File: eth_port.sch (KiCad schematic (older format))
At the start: 19 parts, among them U201 LAN8810

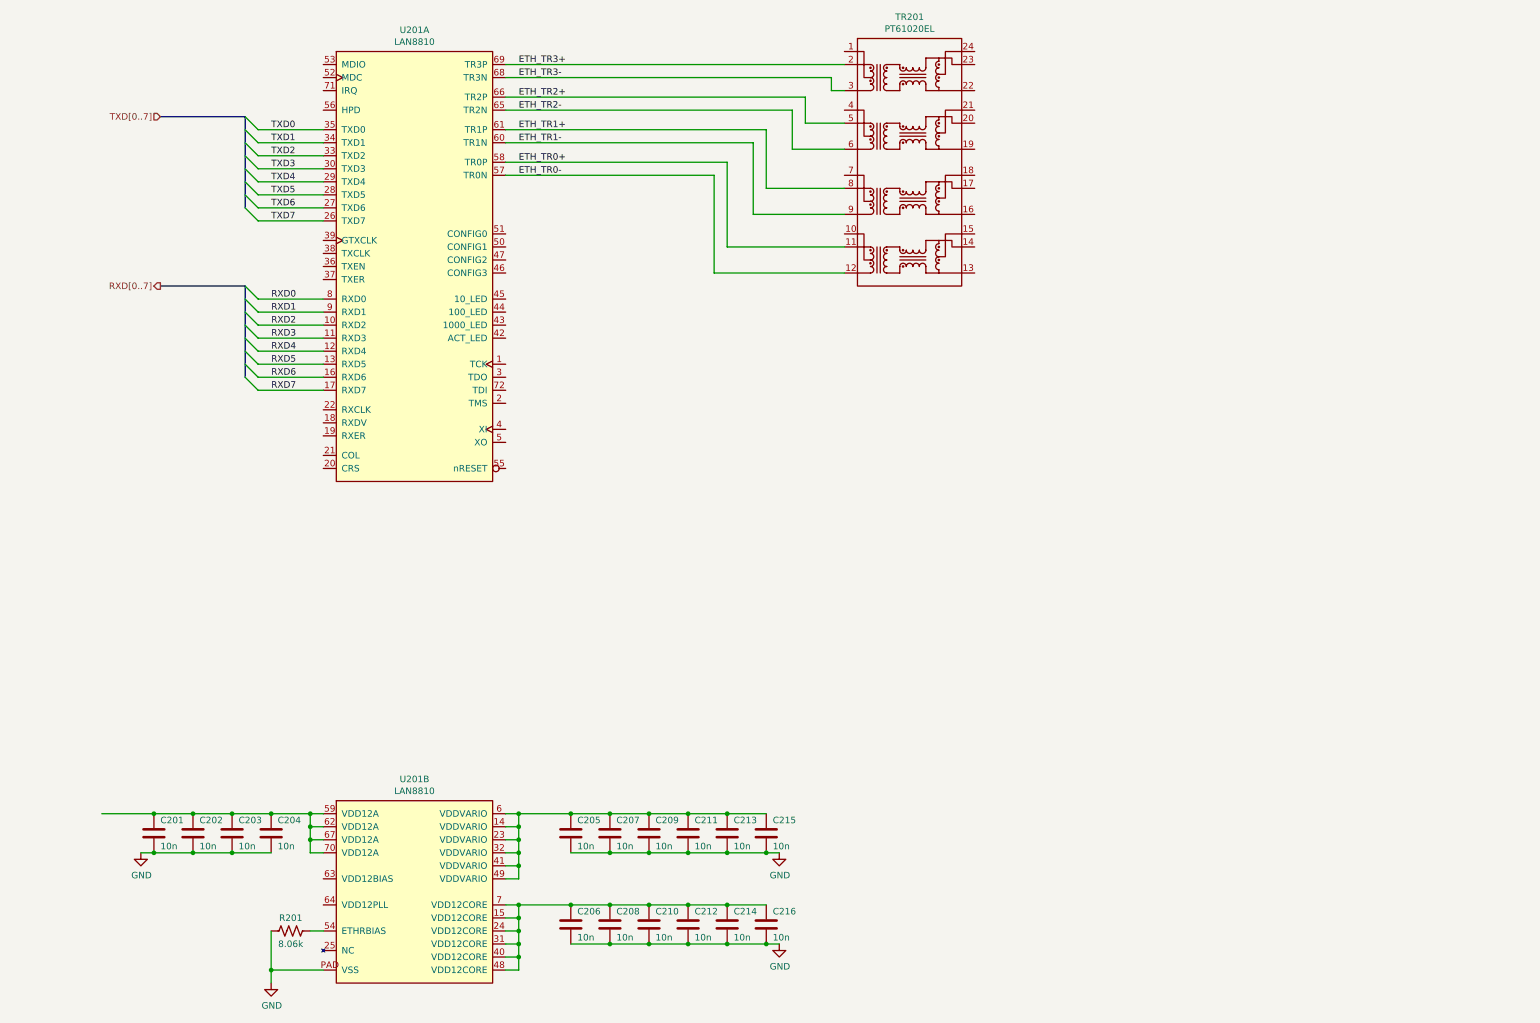
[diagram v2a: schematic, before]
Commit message: - Selected a shielded RJ45 with dual LEDs, with the cable orientation such   that it makes the transformer-to-RJ45 wiring nice. - Added a second whole Ethernet port and connected the two ports together at   the top level.
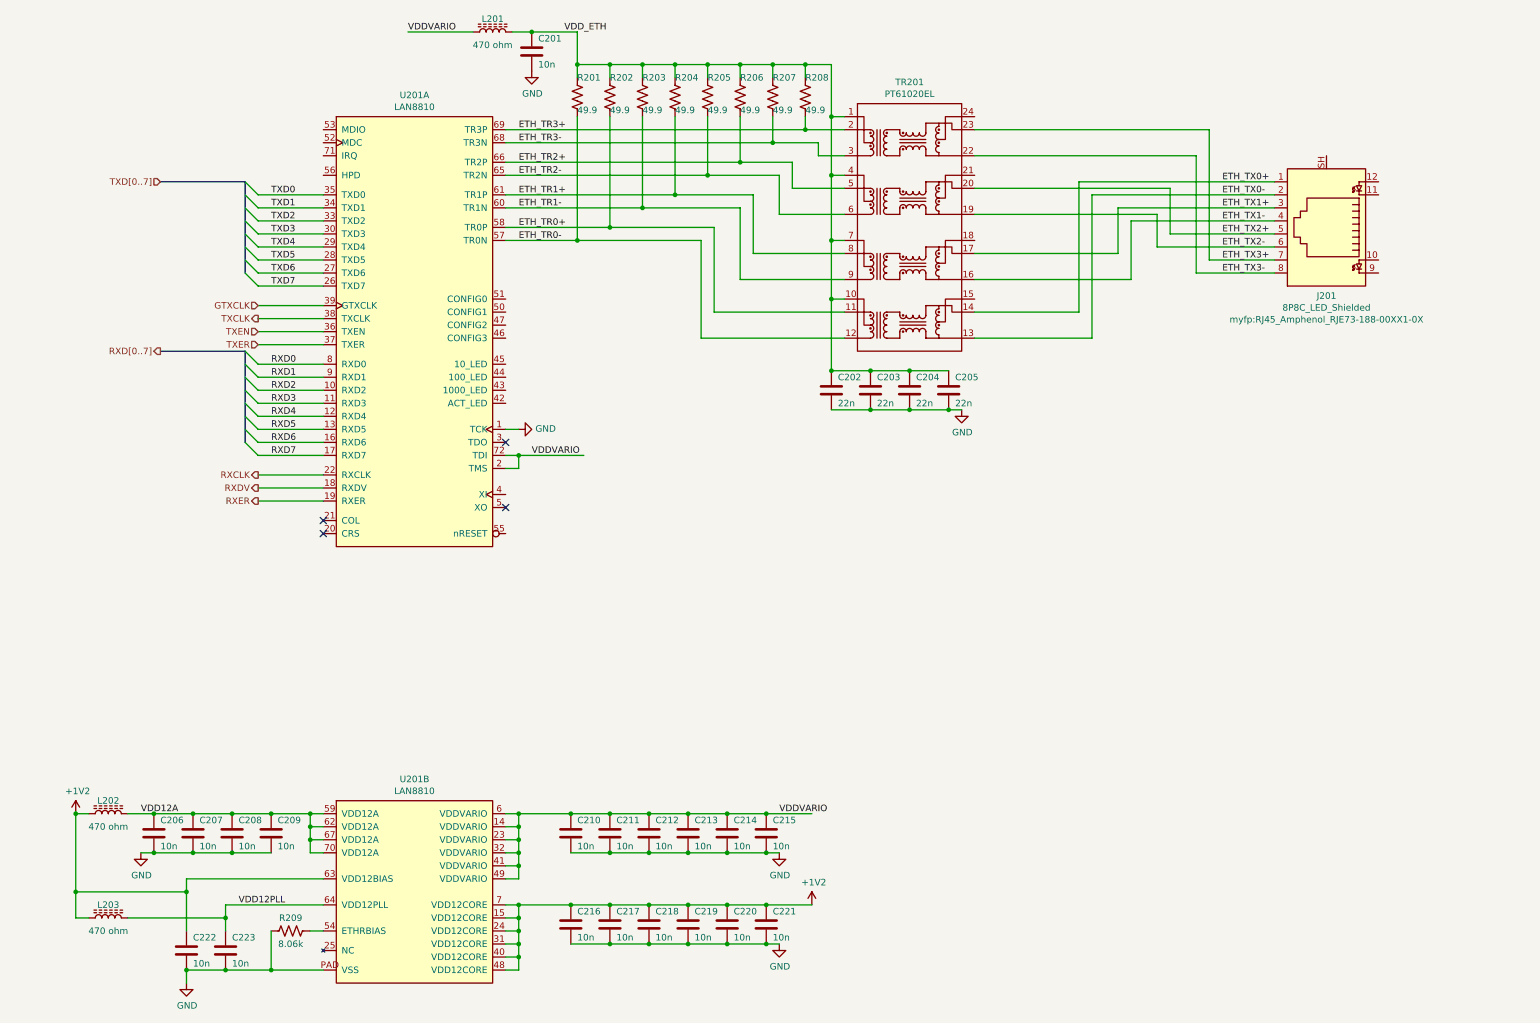
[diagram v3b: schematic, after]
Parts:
- added C301, C322, C323: 10n, Capacitor_SMD:C_0603_1608Metric, symbol Device:C
- added C302, C303, C304, C305: 22n, Capacitor_SMD:C_0603_1608Metric, symbol Device:C
- added J301: 8P8C_LED_Shielded, myfp:RJ45_Amphenol_RJE73-188-00XX1-0X, symbol Connector:8P8C_LED_Shielded
- added L301, L302, L303: 470 ohm, Inductor_SMD:L_0603_1608Metric, symbol Device:L_Core_Ferrite
- added R301, R302, R303, R304, R305, R306, R307, R308: 49.9, Resistor_SMD:R_0603_1608Metric, symbol Device:R_US
- renumbered C201 to C306, C202 to C307, C203 to C308, C204 to C309, C205 to C310, C207 to C311, C209 to C312, C211 to C313, C213 to C314, C215 to C315, C206 to C316, C208 to C317, C210 to C318, C212 to C319, C214 to C320, C216 to C321, R201 to R309, TR201 to TR301, U201 to U301
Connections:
- net ETH_TR0+: now also R302.2
- net ETH_TR0-: now also R301.2
- net ETH_TR1+: now also R304.2
- net ETH_TR1-: now also R303.2
- net ETH_TR2+: now also R306.2
- net ETH_TR2-: now also R305.2
- net ETH_TR3+: now also R308.2
- net ETH_TR3-: now also R307.2
- net GND: now also U301.1 (TCK), C301.2, C302.2, C303.2, C304.2, C305.2, C322.2, C323.2
- net RXDV: now reaches U301.18 (RXDV)
- net RXER: now reaches U301.19 (RXER)
- net VDDVARIO: now reaches U301.2 (TMS)
- net VDDVARIO: now also C310.1, C311.1, C312.1, C313.1, C314.1, C315.1, U301.14 (VDDVARIO), U301.23 (VDDVARIO), U301.32 (VDDVARIO), U301.41 (VDDVARIO), U301.49 (VDDVARIO), U301.6 (VDDVARIO), U301.72 (TDI), L301.1
- net RXCLK: now reaches U301.22 (RXCLK)
- net TXEN: now reaches U301.36 (TXEN)
- net TXER: now reaches U301.37 (TXER)
- net TXCLK: now reaches U301.38 (TXCLK)
- net GTXCLK: now reaches U301.39 (GTXCLK)
- net +1V2: now reaches C316.1, C317.1, C318.1, C319.1, C320.1, C321.1, U301.15 (VDD12CORE), U301.24 (VDD12CORE), U301.31 (VDD12CORE), U301.40 (VDD12CORE), U301.48 (VDD12CORE), U301.7 (VDD12CORE)
- net +1V2: now also U301.63 (VDD12BIAS), C322.1, L302.1, L303.1
- net VDD12A: now reaches C306.1, C307.1, C308.1, C309.1, U301.59 (VDD12A), U301.62 (VDD12A), U301.67 (VDD12A), U301.70 (VDD12A)
- net VDD12A: now also L302.2
- net VDD12PLL: now reaches U301.64 (VDD12PLL)
- net VDD12PLL: now also C323.1, L303.2
- net VDD_ETH: now reaches TR301.1 (TCT1)
- net VDD_ETH: now also TR301.10 (TCT4), TR301.4 (TCT2), TR301.7 (TCT3), C301.1, C302.1, C303.1, C304.1, C305.1, L301.2, R301.1, R302.1, R303.1, R304.1, R305.1, R306.1, R307.1, R308.1
- net ETH_TX0-: now reaches TR301.13 (MX4-)
- net ETH_TX0-: now also J301.2
- net ETH_TX0+: now reaches TR301.14 (MX4+)
- net ETH_TX0+: now also J301.1
- net ETH_TX1-: now reaches TR301.16 (MX3-)
- net ETH_TX1-: now also J301.4
- net ETH_TX1+: now reaches TR301.17 (MX3+)
- net ETH_TX1+: now also J301.3
- net ETH_TX2-: now reaches TR301.19 (MX2-)
- net ETH_TX2-: now also J301.6
- net ETH_TX2+: now reaches TR301.20 (MX2+)
- net ETH_TX2+: now also J301.5
- net ETH_TX3-: now reaches TR301.22 (MX1-)
- net ETH_TX3-: now also J301.8
- net ETH_TX3+: now reaches TR301.23 (MX1+)
- net ETH_TX3+: now also J301.7
- no-connect marks 0 -> 4
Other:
- moved on the sheet: TR201, U201A

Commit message: - Added termination network to line side of Ethernet transformer - Started vaguely laying out the big pieces of Ethernet1 block - Set PCB layout to be six layers - Added layout layer identification texts
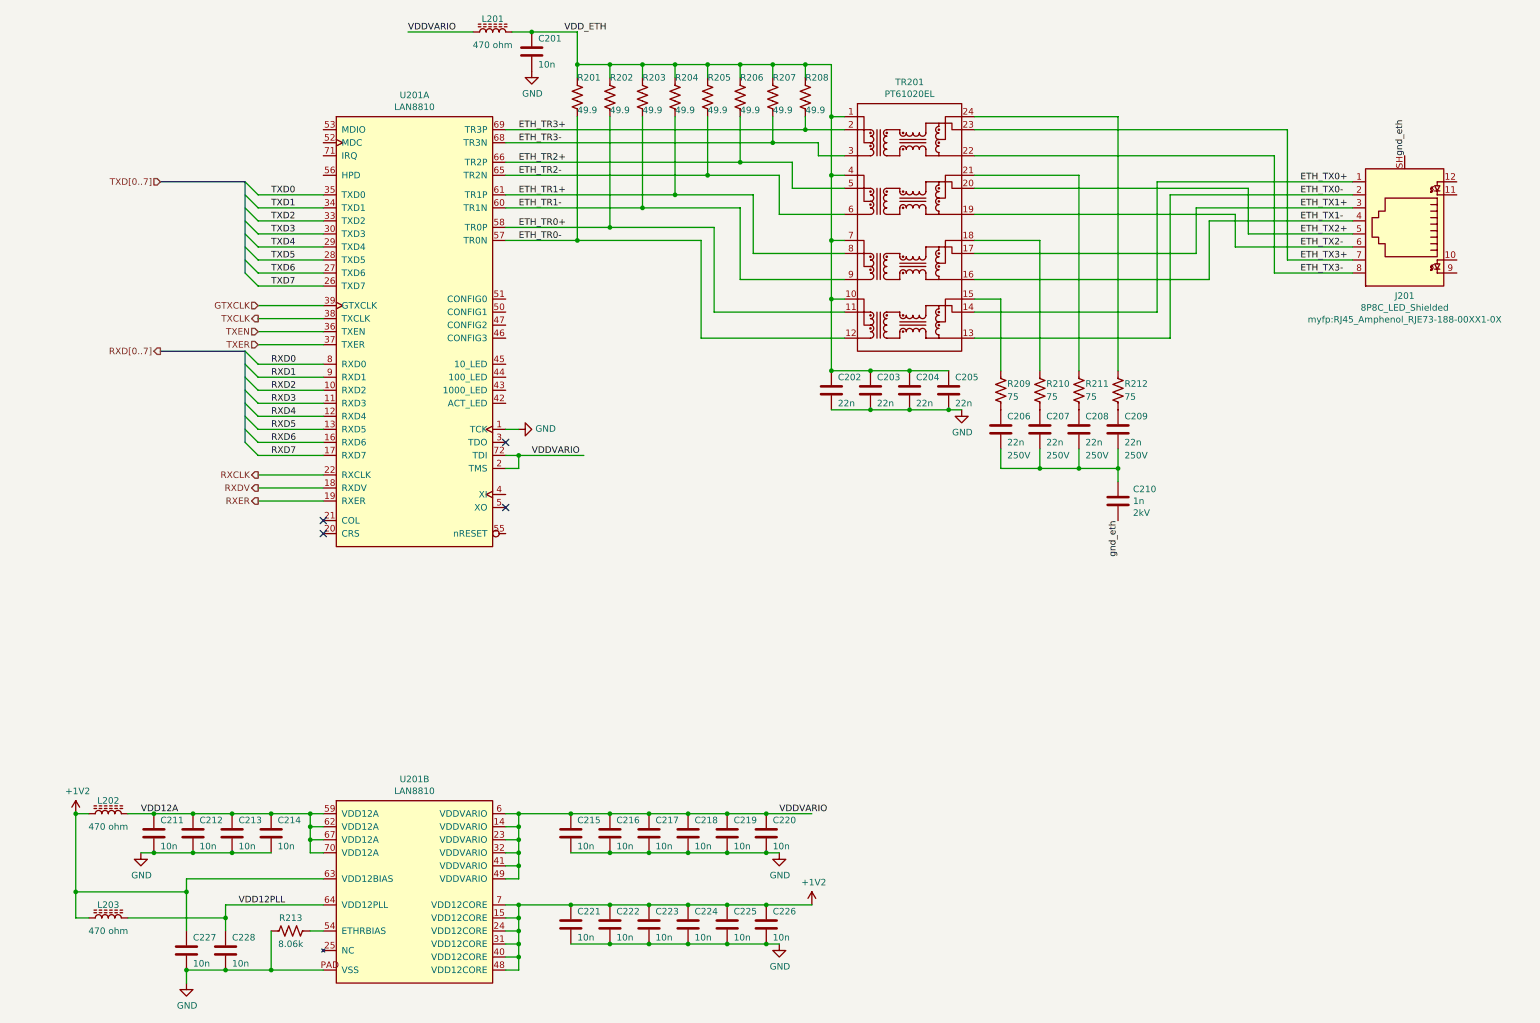
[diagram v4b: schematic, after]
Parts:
- added C206, C207, C208, C209: 22n, Capacitor_SMD:C_0805_2012Metric, symbol Device:C
- added C210: 1n, Capacitor_SMD:C_1206_3216Metric, symbol Device:C
- added R209, R210, R211, R212: 75, Resistor_SMD:R_0603_1608Metric, symbol Device:R_US
- renumbered C306 to C311, C307 to C312, C308 to C313, C309 to C314, C310 to C315, C311 to C316, C312 to C317, C313 to C318, C314 to C319, C315 to C320, C316 to C321, C317 to C322, C318 to C323, C319 to C324, C320 to C325, C321 to C326, C322 to C327, C323 to C328, R309 to R313
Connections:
- net at TR301.15 (MCT4): now also R209.1
- net at TR301.18 (MCT3): now also R210.1
- net at TR301.21 (MCT2): now also R211.1
- net at TR301.24 (MCT1): now also R212.1
- net gnd_eth: now reaches J301.SH
- net gnd_eth: now also C210.2
- new net: C206.1, R209.2
- new net: C206.2, C207.2, C208.2, C209.2, C210.1
- new net: C207.1, R210.2
- new net: C208.1, R211.2
- new net: C209.1, R212.2
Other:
- moved on the sheet: J201

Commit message: - Adjusted RJ45 main pin thru-holes to have only an 8mil-wide ring, instead of   10mil.  There was just not enough room for routing. - Fixed wiring to RJ45, it was 3/4 and 5/6 instead of 3/6 and 4/5, whoops! - Set up basic board routing parameters including diff pairs - Routed the Ethernet1 transformer-to-RJ45 area as proof-of-concept
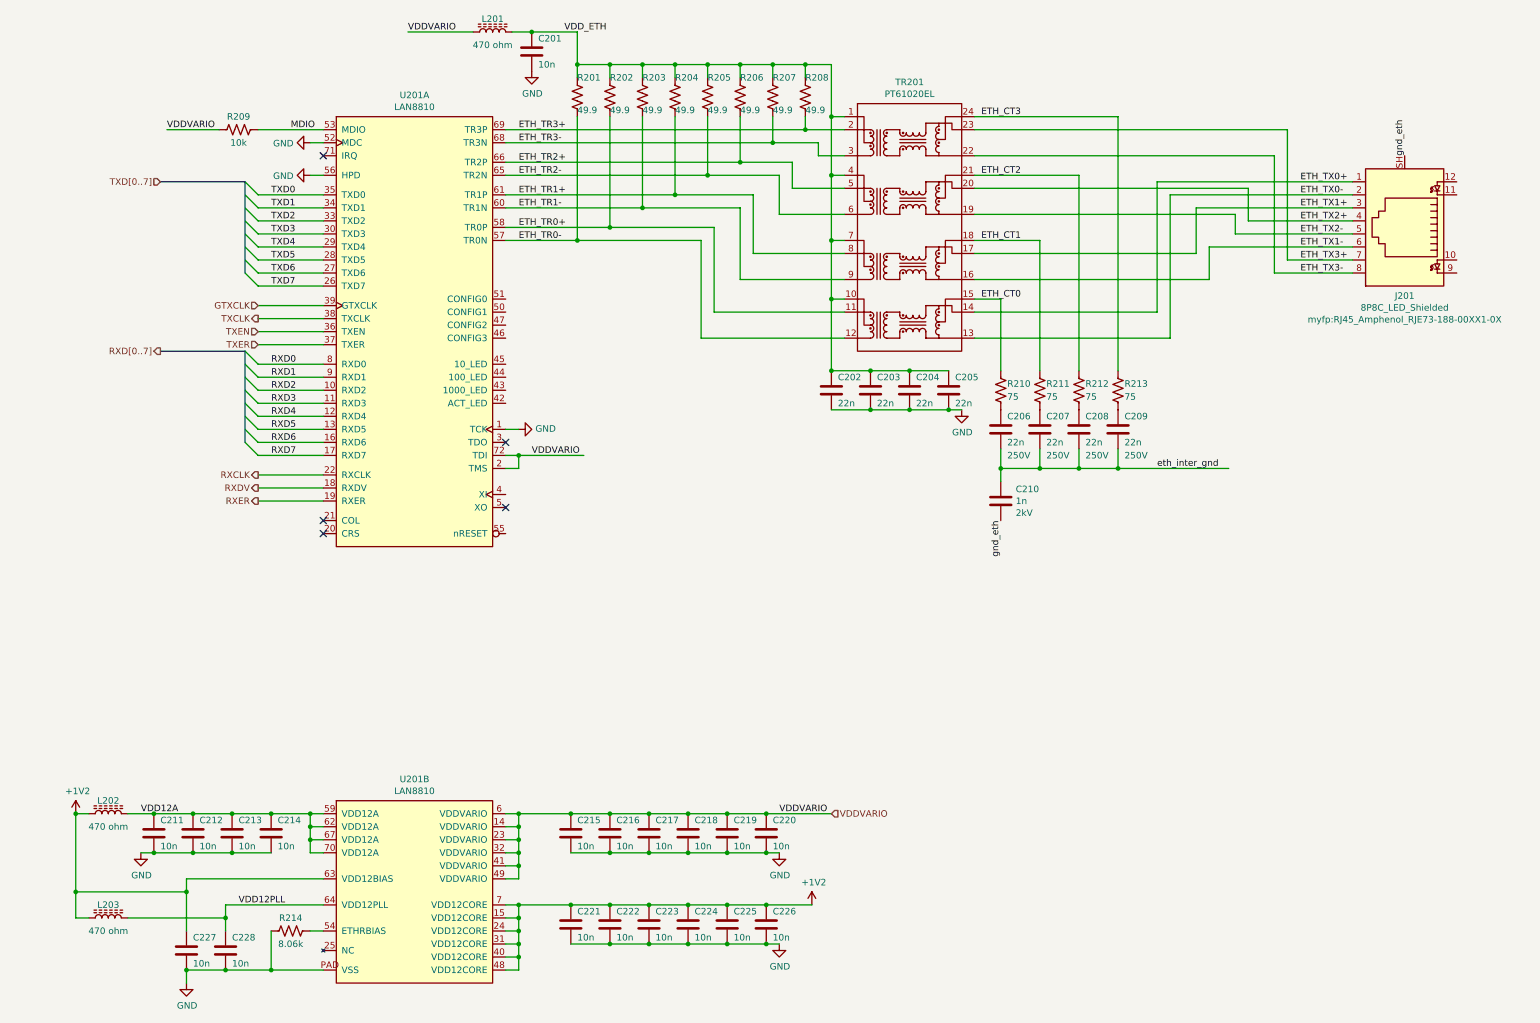
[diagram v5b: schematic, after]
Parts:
- added R209: 10k, Resistor_SMD:R_0603_1608Metric, symbol Device:R_US
- renumbered R209 to R210, R210 to R211, R211 to R212, R212 to R213, R313 to R314
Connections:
- net ETH_TX1-: now also J301.6; no longer J301.4
- net ETH_TX2+: now also J301.4; no longer J301.5
- net ETH_TX2-: now also J301.5; no longer J301.6
- net GND: now also U301.52 (MDC), U301.56 (HPD)
- net VDDVARIO: now also R209.2
- net MDIO: now reaches U301.53 (MDIO)
- net MDIO: now also R209.1
- net ETH_CT0: now reaches R210.1, TR301.15 (MCT4)
- net ETH_CT1: now reaches R211.1, TR301.18 (MCT3)
- net ETH_CT2: now reaches R212.1, TR301.21 (MCT2)
- net ETH_CT3: now reaches R213.1, TR301.24 (MCT1)
- net eth_inter_gnd: now reaches C206.2, C207.2, C208.2, C209.2, C210.1
- no-connect marks 4 -> 5
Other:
- moved on the sheet: C210
